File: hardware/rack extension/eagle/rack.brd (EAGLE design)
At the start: 160 x 100 mm, 48 parts, among them IC1 74ACT139N, IC2 74AC574N, IC3 74AC32N, IC4 74AC86N, IC5 74AC04N, IC6 74AC14N, IC7 74AC541N, K1 APF30212C, K2 APF30212C, Q1 BC547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

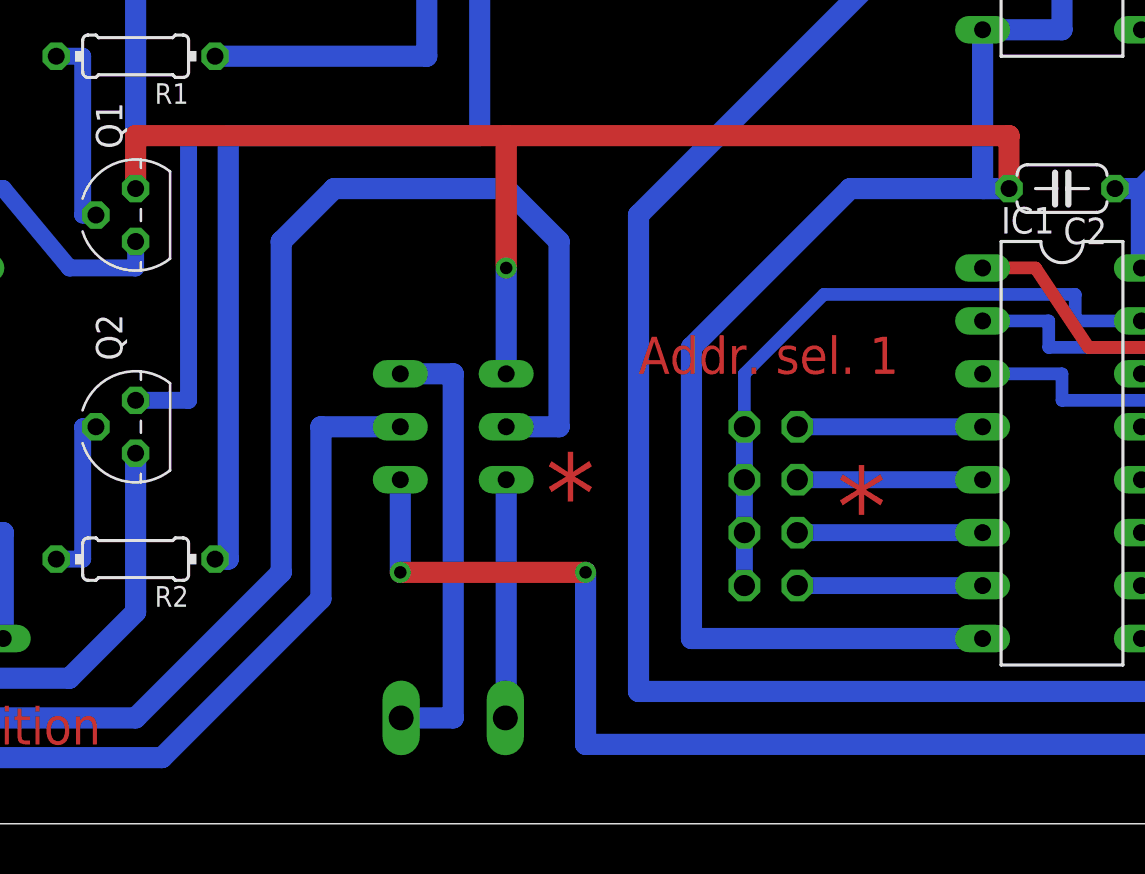
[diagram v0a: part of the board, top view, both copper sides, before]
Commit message: Bad fail in rack hardware
The switch S1 was connected wrong so the change from internal to
external supply didnt work.
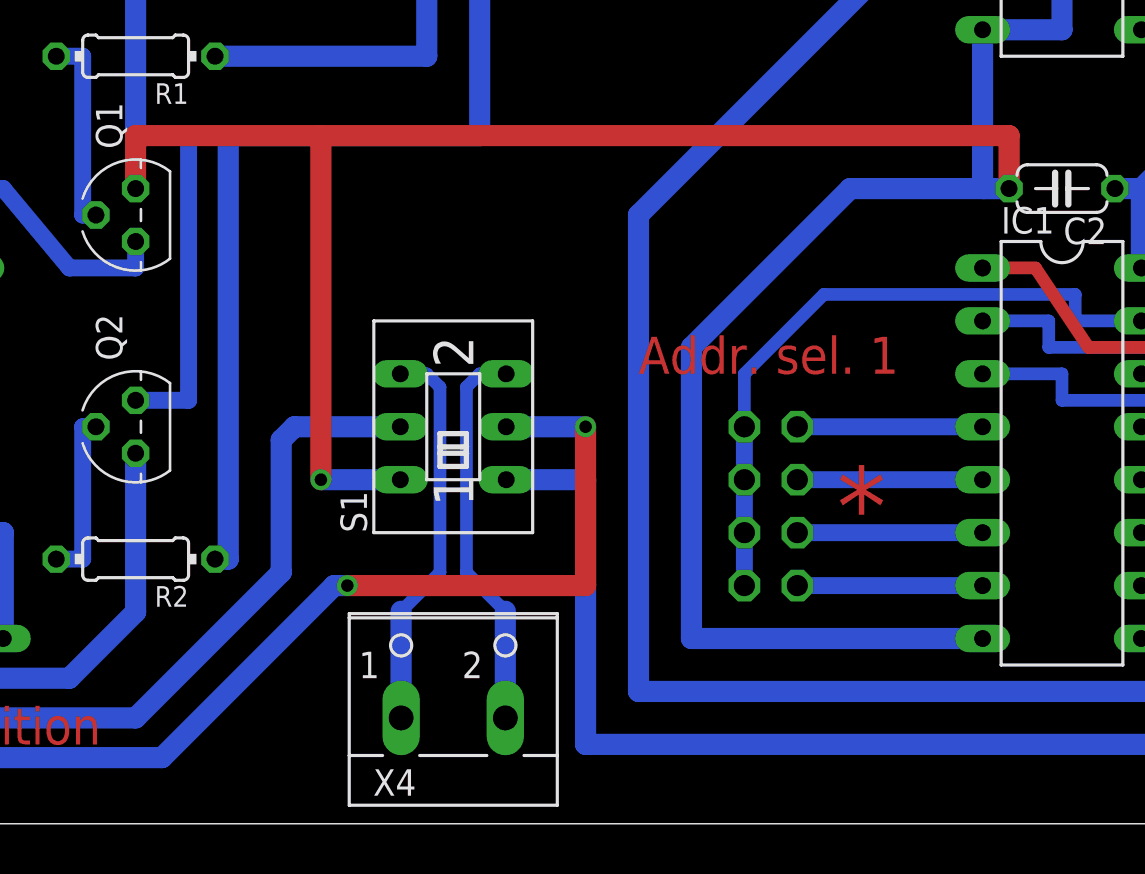
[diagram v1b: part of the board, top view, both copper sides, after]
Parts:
- flipped S1 to the top
- flipped X4 to the top
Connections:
- net GND: now also S1.4; no longer S1.6
- net N$33: now also S1.6; no longer S1.4
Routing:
- net N$27: track 89.0 -> 58.6 mm
- net N$34: track 66.1 -> 78.4 mm, vias 0 -> 2
- net GND: track 709.1 -> 718.0 mm
- net N$33: track 11.5 -> 18.9 mm, vias 0 -> 1
- net +12V: track 115.9 -> 110.8 mm, vias 2 -> 0
- net N$32: track 21.6 -> 18.9 mm, vias 0 -> 1

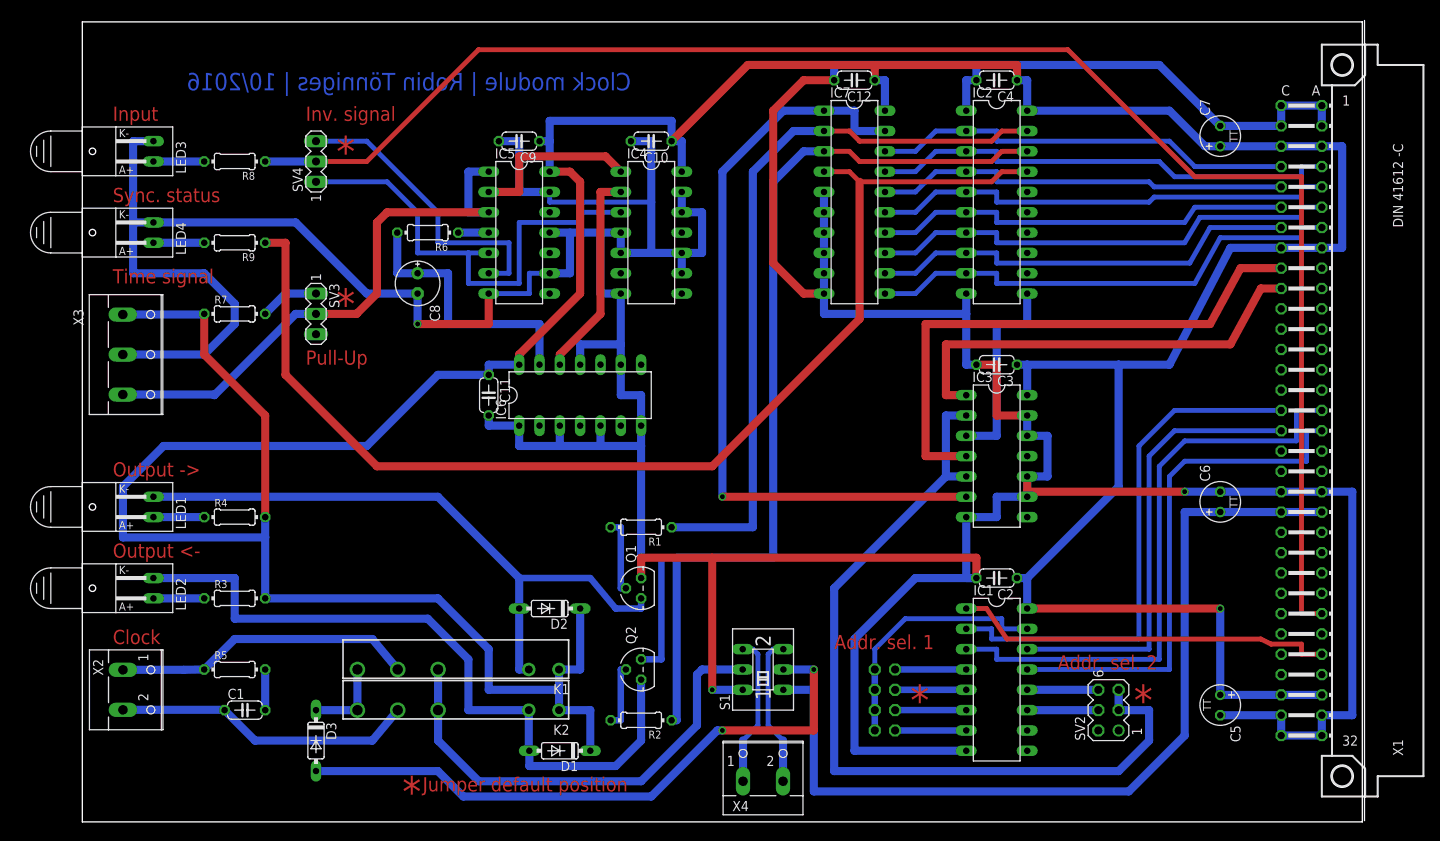
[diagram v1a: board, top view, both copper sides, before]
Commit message: Layout updated
Updated layout from rack extension
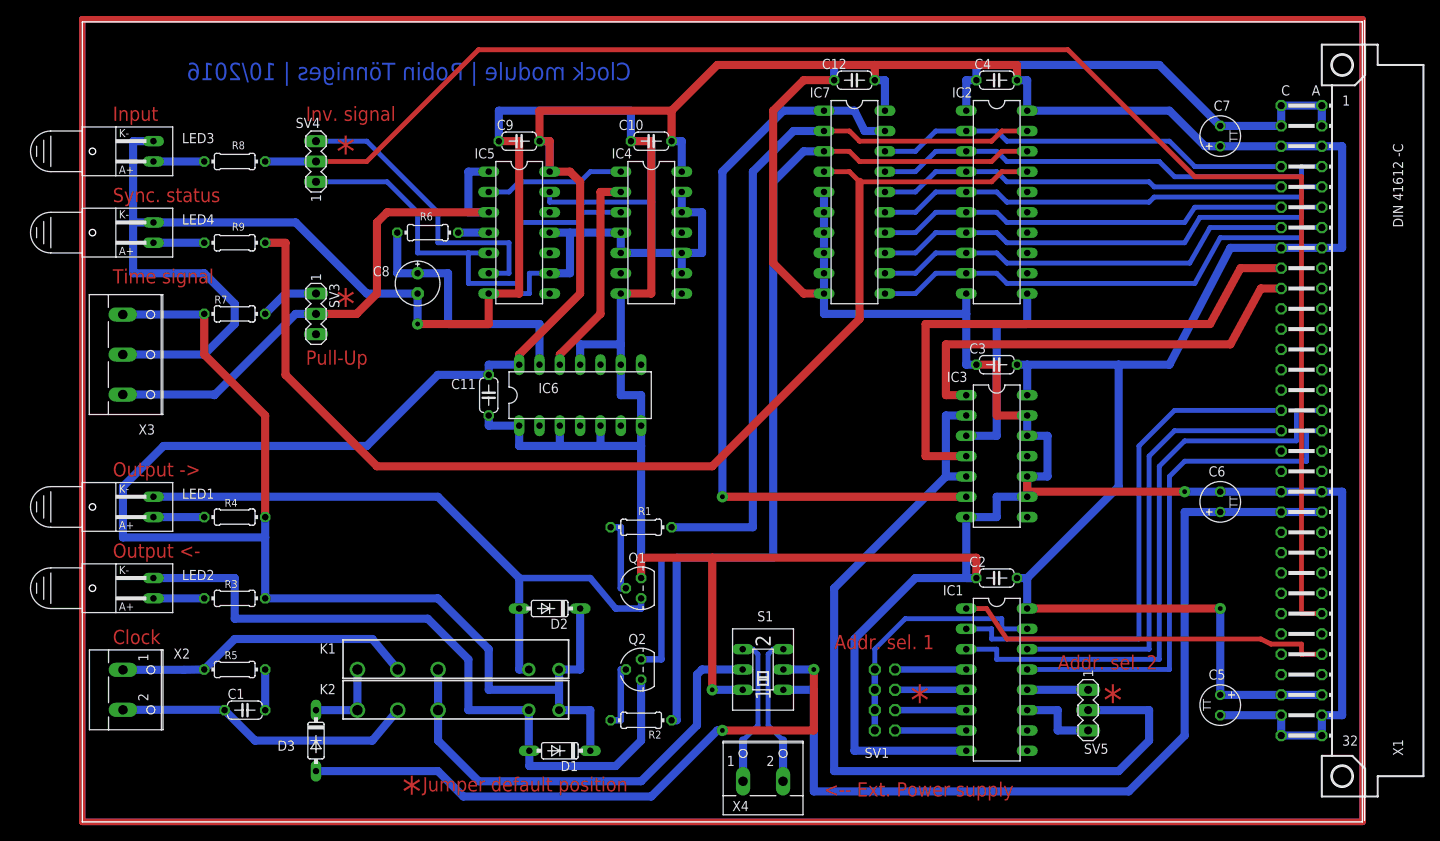
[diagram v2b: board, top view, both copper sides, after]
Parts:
- removed SV2: (no value), con-lstb:MA03-2
- added SV5: (no value), con-lstb:MA03-1
- C8: value (none) -> 2µ2
- IC1: value 74ACT139N -> 74HC139N
- IC2: value 74AC574N -> 74HC574N
- IC3: value 74AC32N -> 74HC32N
- IC4: value 74AC86N -> 74HC86N
- IC5: value 74AC04N -> 74HC04N
- IC6: value 74AC14N -> 74HC14N
- IC7: value 74AC541N -> 74HC541N
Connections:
- net N$36: now also SV5.2; no longer SV2.3, SV2.5
- net N$6: now also SV5.3; no longer SV2.4
- net N$7: now also SV5.1; no longer SV2.6
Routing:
- net N$39: track 0.00 -> 520.7 mm
- net N$38: track 0.00 -> 520.7 mm
- net GND: track 718.0 -> 767.5 mm
- net VCC: track 511.7 -> 519.0 mm
- net N$24: track 21.7 -> 17.6 mm
- net N$6: track 8.89 -> 10.2 mm
- net N$7: track 8.89 -> 7.62 mm
- net N$36: track 106.4 -> 107.7 mm
- net N$35: track 97.1 -> 96.2 mm
- net D6: track 54.4 -> 53.7 mm
- net D7: track 61.6 -> 60.8 mm
- net D5: track 60.0 -> 59.3 mm
- net D4: track 52.9 -> 52.1 mm
- net D3: track 58.5 -> 57.7 mm
- net D2: track 52.1 -> 51.4 mm
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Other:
- board text added: "<-- Ext. Power supply"

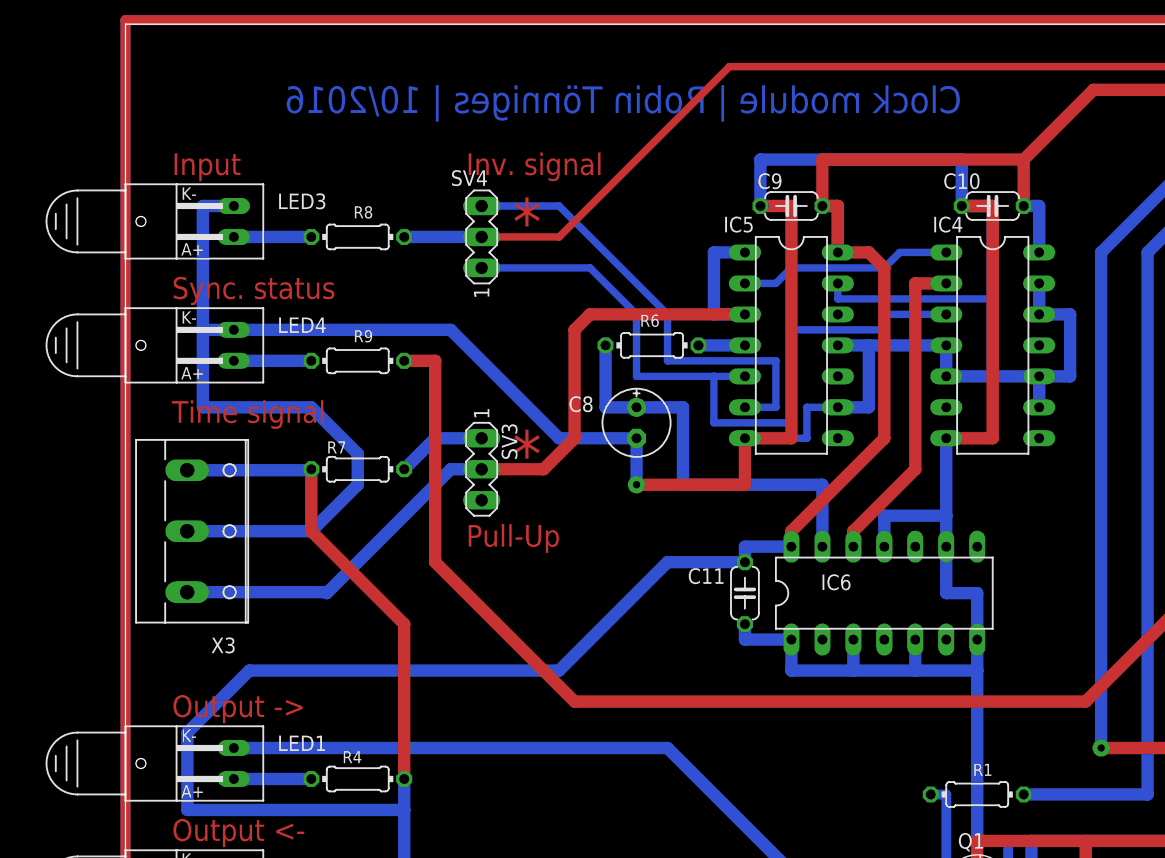
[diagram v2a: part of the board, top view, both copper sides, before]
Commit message: Litte changes in schematic and layout
Added further description and fixed an naming issue in schmematic
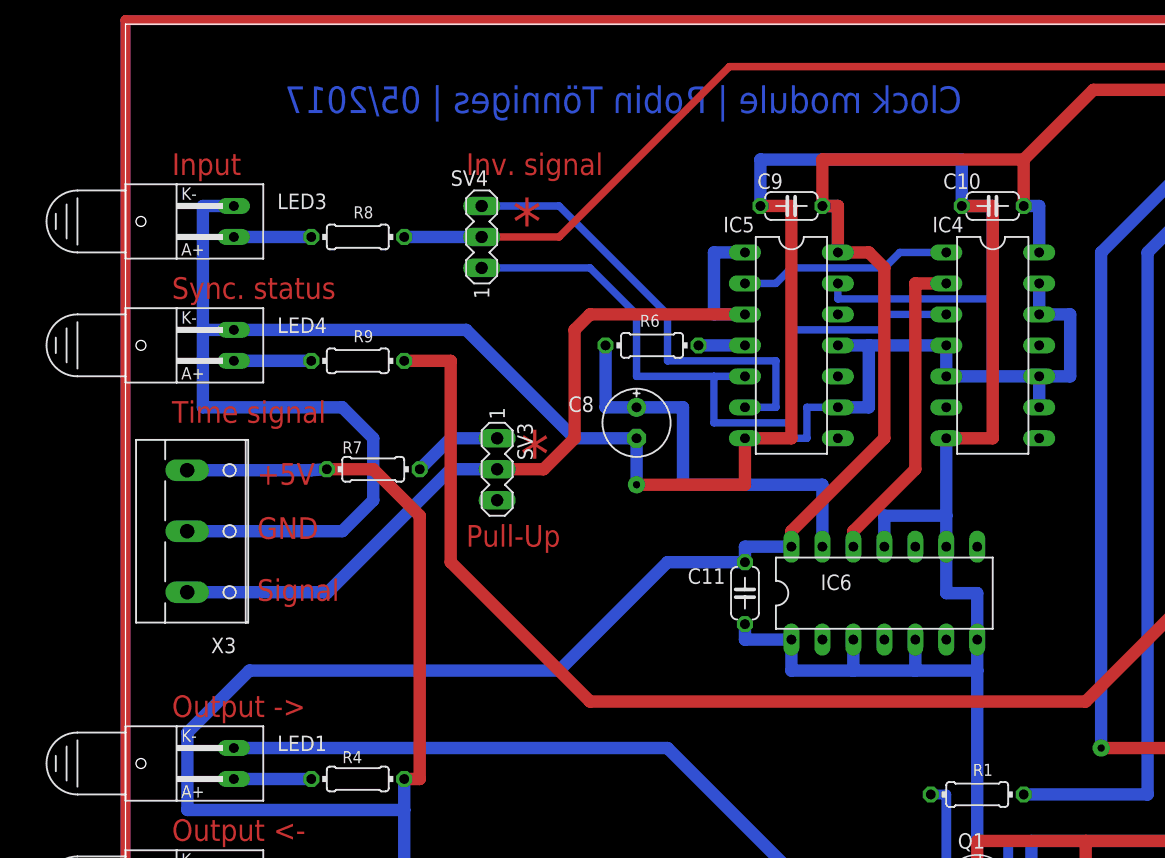
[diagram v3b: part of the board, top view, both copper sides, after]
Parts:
- moved R7 1.27 mm to (20.3, 63.5)
- moved SV3 1.27 mm to (30.5, 63.5)
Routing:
- net VCC: track 519.0 -> 523.7 mm
- net GND: track 767.5 -> 771.6 mm
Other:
- board text added: "+5V"
- board text added: "Clock module | Robin Tönniges | 05/2017"
- board text added: "GND"
- board text added: "Signal"
- board text removed: "Clock module | Robin Tönniges | 10/2016"
